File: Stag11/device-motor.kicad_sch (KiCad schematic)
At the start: 2 parts

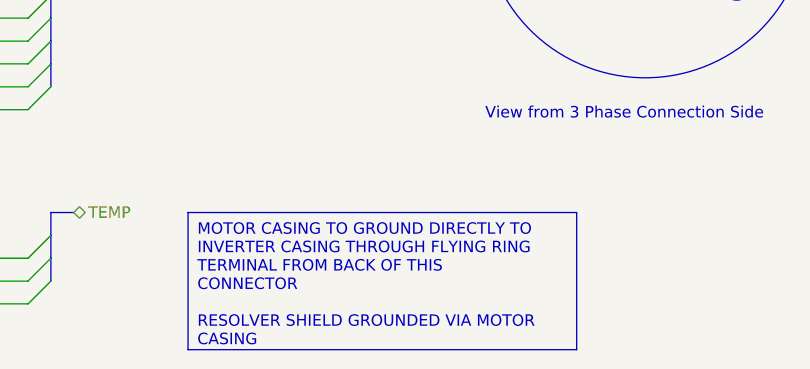
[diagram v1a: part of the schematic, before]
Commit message: Fixed mislabelled wires for precharge
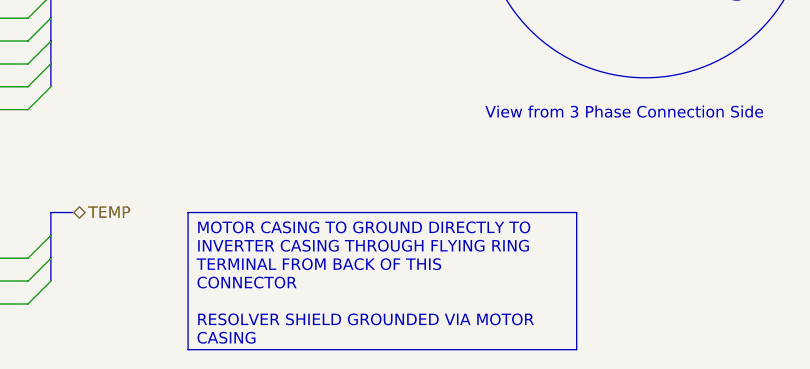
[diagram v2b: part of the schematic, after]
